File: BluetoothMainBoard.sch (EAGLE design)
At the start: 32 parts, among them IC1 MCP73831, J1 J_USB_MICROAB_HIROSE_ZX62-AB-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, U1 MAX921MSA/PR

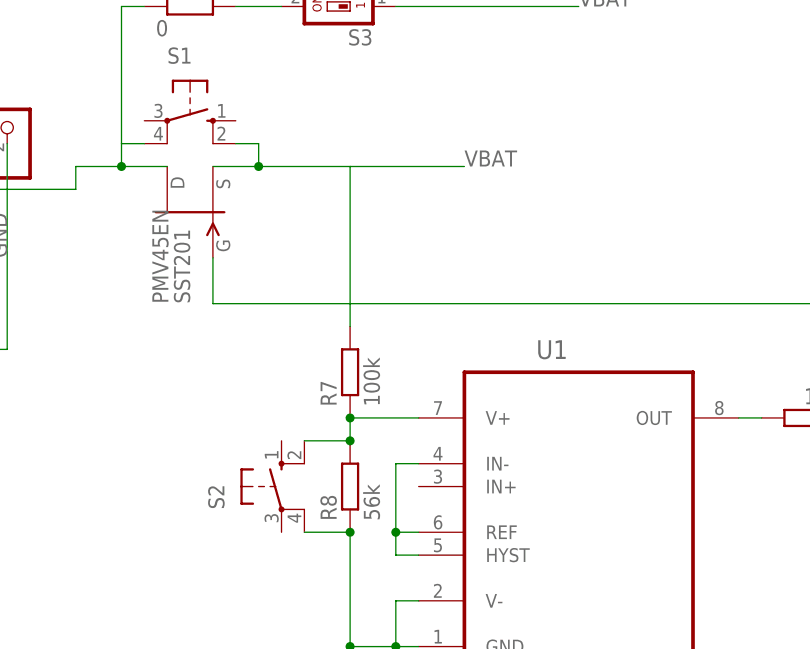
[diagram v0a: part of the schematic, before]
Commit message: rewire for max921
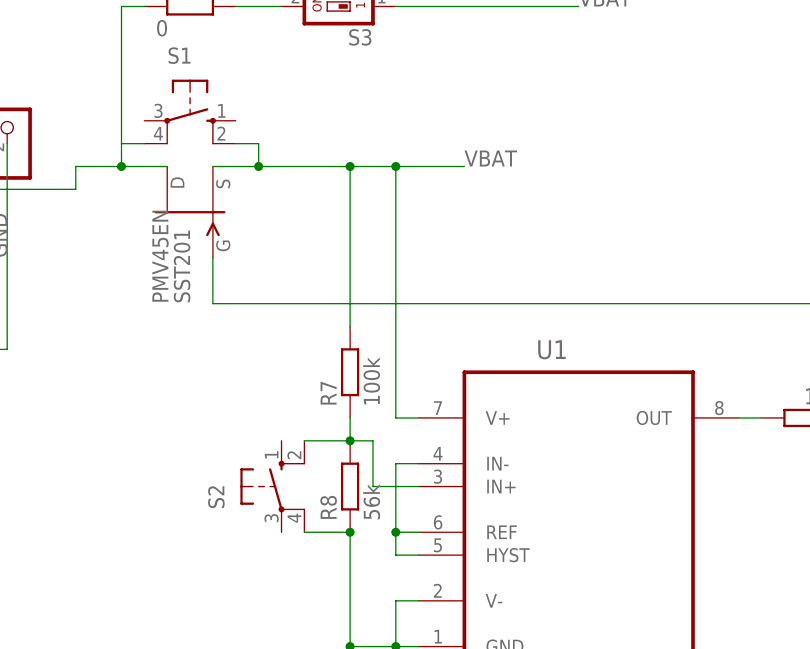
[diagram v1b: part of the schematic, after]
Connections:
- net N$18: now also U1.IN+; no longer U1.V+
- net VBAT: now also U1.V+
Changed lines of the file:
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@@
 <grid distance="0.1" unitdist="inch" unit="inch" style="lines" multiple="1" display="no" altdistance="0.01" altunitdist="inch" altunit="inch"/>
 <layers>
-<layer number="1" name="Top" color="4" fill="1" visible="yes" active="no"/>
-<layer number="2" name="Route2" color="1" fill="3" visible="yes" active="no"/>
-<layer number="3" name="Route3" color="4" fill="3" visible="yes" active="no"/>
-<layer number="4" name="Route4" color="1" fill="4" visible="yes" active="no"/>
-<layer number="5" name="Route5" color="4" fill="4" visible="yes" active="no"/>
-<layer number="6" name="Route6" color="1" fill="8" visible="yes" active="no"/>
-<layer number="7" name="Route7" color="4" fill="8" visible="yes" active="no"/>
-<layer number="8" name="Route8" color="1" fill="2" visible="yes" active="no"/>
-<layer number="9" name="Route9" color="4" fill="2" visible="yes" active="no"/>
-<layer number="10" name="Route10" color="1" fill="7" visible="yes" active="no"/>
-<layer number="11" name="Route11" color="4" fill="7" visible="yes" active="no"/>
-<layer number="12" name="Route12" color="1" fill="5" visible="yes" active="no"/>
-<layer number="13" name="Route13" color="4" fill="5" visible="yes" active="no"/>
-<layer number="14" name="Route14" color="1" fill="6" visible="yes" active="no"/>
-<layer number="15" name="Route15" color="4" fill="6" visible="yes" active="no"/>
-<layer number="16" name="Bottom" color="1" fill="1" visible="yes" active="no"/>
-<layer number="17" name="Pads" color="2" fill="1" visible="yes" active="no"/>
-<layer number="18" name="Vias" color="2" fill="1" visible="yes" active="no"/>
-<layer number="19" name="Unrouted" color="6" fill="1" visible="yes" active="no"/>
-<layer number="20" name="Dimension" color="15" fill="1" visible="yes" active="no"/>
-<layer number="21" name="tPlace" color="7" fill="1" visible="yes" active="no"/>
-<layer number="22" name="bPlace" color="7" fill="1" visible="yes" active="no"/>
-<layer number="23" name="tOrigins" color="15" fill="1" visible="yes" active="no"/>
-<layer number="24" name="bOrigins" color="15" fill="1" visible="yes" active="no"/>
-<layer number="25" name="tNames" color="7" fill="1" visible="yes" active="no"/>
-<layer number="26" name="bNames" color="7" fill="1" visible="yes" active="no"/>
-<layer number="27" name="tValues" color="7" fill="1" visible="yes" active="no"/>
-<layer number="28" name="bValues" color="7" fill="1" visible="yes" active="no"/>
+<layer number="1" name="Top" color="4" fill="1" visible="no" active="no"/>
+<layer number="2" name="Route2" color="1" fill="3" visible="no" active="no"/>
+<layer number="3" name="Route3" color="4" fill="3" visible="no" active="no"/>
+<layer number="4" name="Route4" color="1" fill="4" visible="no" active="no"/>
+<layer number="5" name="Route5" color="4" fill="4" visible="no" active="no"/>
+<layer number="6" name="Route6" color="1" fill="8" visible="no" active="no"/>
+<layer number="7" name="Route7" color="4" fill="8" visible="no" active="no"/>
+<layer number="8" name="Route8" color="1" fill="2" visible="no" active="no"/>
+<layer number="9" name="Route9" color="4" fill="2" visible="no" active="no"/>
+<layer number="10" name="Route10" color="1" fill="7" visible="no" active="no"/>
+<layer number="11" name="Route11" color="4" fill="7" visible="no" active="no"/>
+<layer number="12" name="Route12" color="1" fill="5" visible="no" active="no"/>
+<layer number="13" name="Route13" color="4" fill="5" visible="no" active="no"/>
+<layer number="14" name="Route14" color="1" fill="6" visible="no" active="no"/>
+<layer number="15" name="Route15" color="4" fill="6" visible="no" active="no"/>
+<layer number="16" name="Bottom" color="1" fill="1" visible="no" active="no"/>
+<layer number="17" name="Pads" color="2" fill="1" visible="no" active="no"/>
+<layer number="18" name="Vias" color="2" fill="1" visible="no" active="no"/>
+<layer number="19" name="Unrouted" color="6" fill="1" visible="no" active="no"/>
+<layer number="20" name="Dimension" color="15" fill="1" visible="no" active="no"/>
+<layer number="21" name="tPlace" color="7" fill="1" visible="no" active="no"/>
+<layer number="22" name="bPlace" color="7" fill="1" visible="no" active="no"/>
+<layer number="23" name="tOrigins" color="15" fill="1" visible="no" active="no"/>
+<layer number="24" name="bOrigins" color="15" fill="1" visible="no" active="no"/>
+<layer number="25" name="tNames" color="7" fill="1" visible="no" active="no"/>
+<layer number="26" name="bNames" color="7" fill="1" visible="no" active="no"/>
+<layer number="27" name="tValues" color="7" fill="1" visible="no" active="no"/>
+<layer number="28" name="bValues" color="7" fill="1" visible="no" active="no"/>
 <layer number="29" name="tStop" color="7" fill="3" visible="no" active="no"/>
 <layer number="30" name="bStop" color="7" fill="6" visible="no" active="no"/>
@@
 <layer number="35" name="tGlue" color="7" fill="4" visible="no" active="no"/>
 <layer number="36" name="bGlue" color="7" fill="5" visible="no" active="no"/>
-<layer number="37" name="tTest" color="7" fill="1" visible="yes" active="no"/>
-<layer number="38" name="bTest" color="7" fill="1" visible="yes" active="no"/>
+<layer number="37" name="tTest" color="7" fill="1" visible="no" active="no"/>
+<layer number="38" name="bTest" color="7" fill="1" visible="no" active="no"/>
 <layer number="39" name="tKeepout" color="4" fill="11" visible="no" active="no"/>
 <layer number="40" name="bKeepout" color="1" fill="11" visible="no" active="no"/>
@@
 <layer number="44" name="Drills" color="7" fill="1" visible="no" active="no"/>
 <layer number="45" name="Holes" color="7" fill="1" visible="no" active="no"/>
-<layer number="46" name="Milling" color="3" fill="1" visible="yes" active="no"/>
-<layer number="47" name="Measures" color="7" fill="1" visible="yes" active="no"/>
-<layer number="48" name="Document" color="7" fill="1" visible="yes" active="no"/>
-<layer number="49" name="Reference" color="7" fill="1" visible="yes" active="no"/>
-<layer number="50" name="dxf" color="7" fill="1" visible="yes" active="no"/>
-<layer number="51" name="tDocu" color="7" fill="1" visible="yes" active="no"/>
-<layer number="52" name="bDocu" color="7" fill="1" visible="yes" active="no"/>
-<layer number="53" name="tGND_GNDA" color="7" fill="9" visible="yes" active="no"/>
-<layer number="54" name="bGND_GNDA" color="1" fill="9" visible="yes" active="no"/>
-<layer number="56" name="wert" color="7" fill="1" visible="yes" active="no"/>
+<layer number="46" name="Milling" color="3" fill="1" visible="no" active="no"/>
+<layer number="47" name="Measures" color="7" fill="1" visible="no" active="no"/>
+<layer number="48" name="Document" color="7" fill="1" visible="no" active="no"/>
+<layer number="49" name="Reference" color="7" fill="1" visible="no" active="no"/>
+<layer number="50" name="dxf" color="7" fill="1" visible="no" active="no"/>
+<layer number="51" name="tDocu" color="7" fill="1" visible="no" active="no"/>
+<layer number="52" name="bDocu" color="7" fill="1" visible="no" active="no"/>
+<layer number="53" name="tGND_GNDA" color="7" fill="9" visible="no" active="no"/>
+<layer number="54" name="bGND_GNDA" color="1" fill="9" visible="no" active="no"/>
+<layer number="56" name="wert" color="7" fill="1" visible="no" active="no"/>
 <layer number="57" name="tCAD" color="7" fill="1" visible="no" active="no"/>
 <layer number="59" name="tCarbon" color="7" fill="1" visible="no" active="no"/>
@@
 <wire x1="96.52" y1="111.76" x2="91.44" y2="111.76" width="0.1524" layer="91"/>
 <wire x1="106.68" y1="111.76" x2="106.68" y2="93.98" width="0.1524" layer="91"/>
-<wire x1="106.68" y1="111.76" x2="119.38" y2="111.76" width="0.1524" layer="91"/>
+<wire x1="106.68" y1="111.76" x2="111.76" y2="111.76" width="0.1524" layer="91"/>
 <label x="119.38" y="111.76" size="1.778" layer="95"/>
 <pinref part="S1" gate="1" pin="S1"/>
+<wire x1="111.76" y1="111.76" x2="119.38" y2="111.76" width="0.1524" layer="91"/>
 <wire x1="93.98" y1="114.3" x2="96.52" y2="114.3" width="0.1524" layer="91"/>
 <wire x1="96.52" y1="114.3" x2="96.52" y2="111.76" width="0.1524" layer="91"/>
 <junction x="96.52" y="111.76"/>
+<junction x="106.68" y="111.76"/>
+<pinref part="U1" gate="A" pin="V+"/>
+<wire x1="114.3" y1="83.82" x2="111.76" y2="83.82" width="0.1524" layer="91"/>
+<wire x1="111.76" y1="83.82" x2="111.76" y2="111.76" width="0.1524" layer="91"/>
+<junction x="111.76" y="111.76"/>
 </segment>
 <segment>
@@
 <net name="N$18" class="0">
 <segment>
-<pinref part="U1" gate="A" pin="V+"/>
 <pinref part="R7" gate="G$1" pin="1"/>
 <pinref part="R8" gate="G$1" pin="2"/>
 <wire x1="106.68" y1="83.82" x2="106.68" y2="81.28" width="0.1524" layer="91"/>
-<wire x1="114.3" y1="83.82" x2="106.68" y2="83.82" width="0.1524" layer="91"/>
 <pinref part="S2" gate="1" pin="S1"/>
 <wire x1="101.6" y1="81.28" x2="106.68" y2="81.28" width="0.1524" layer="91"/>
 <junction x="106.68" y="81.28"/>
-<junction x="106.68" y="83.82"/>
-</segment>
-</net>
+<pinref part="U1" gate="A" pin="IN+"/>
+<wire x1="114.3" y1="76.2" x2="109.22" y2="76.2" width="0.1524" layer="91"/>
+<wire x1="109.22" y1="76.2" x2="109.22" y2="81.28" width="0.1524" layer="91"/>
+<wire x1="109.22" y1="81.28" x2="106.68" y2="81.28" width="0.1524" layer="91"/>
+</segment>
+</net>
